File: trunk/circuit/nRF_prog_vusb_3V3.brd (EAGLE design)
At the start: 50 x 50 mm, 34 parts, among them Q1 12MHz

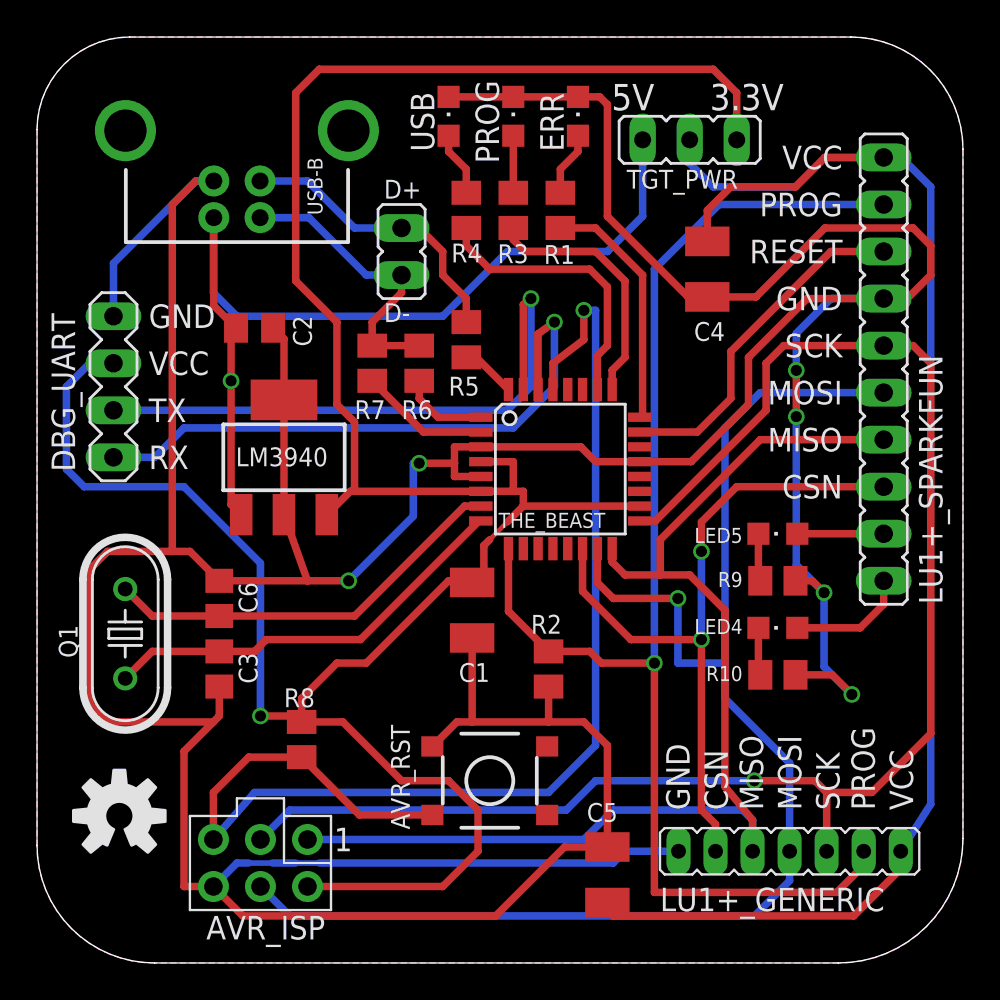
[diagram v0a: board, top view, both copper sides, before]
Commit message: 
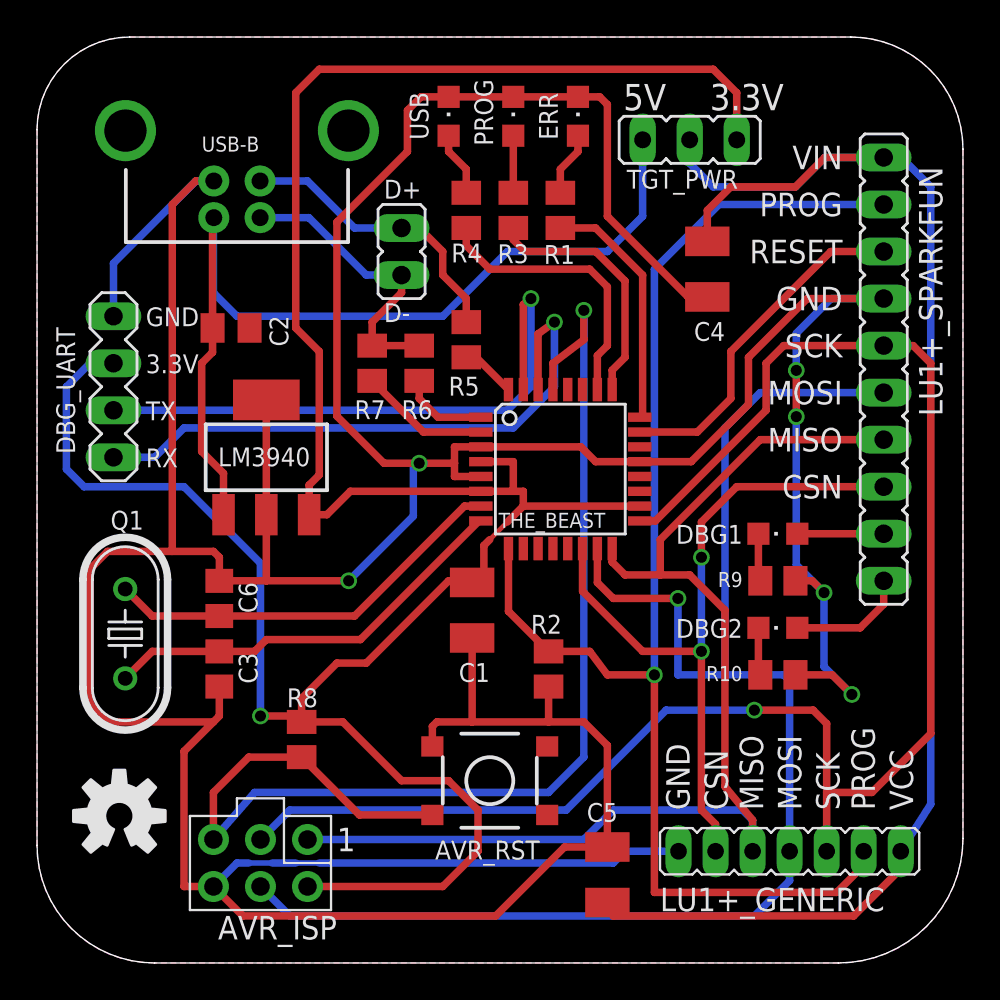
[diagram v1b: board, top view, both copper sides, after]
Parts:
- moved C2 1.27 mm to (10.5, 34.3)
- moved LM3940 0.95 mm to (12.4, 27.3)
- renumbered LED4 to DBG2, LED5 to DBG1
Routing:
- net GND: track 274.2 -> 279.9 mm
- net P0.0: track 83.8 -> 89.1 mm
- net P0.1: track 77.8 -> 80.3 mm
- net 3.3V: track 144.9 -> 146.6 mm
- net AVR_RESET: track 68.5 -> 67.6 mm
- net VBUS: track 51.0 -> 51.3 mm, vias 1 -> 0
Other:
- board text added: "VIN"
